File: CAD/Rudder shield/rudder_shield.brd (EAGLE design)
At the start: 49 x 19.7 mm, 8 parts

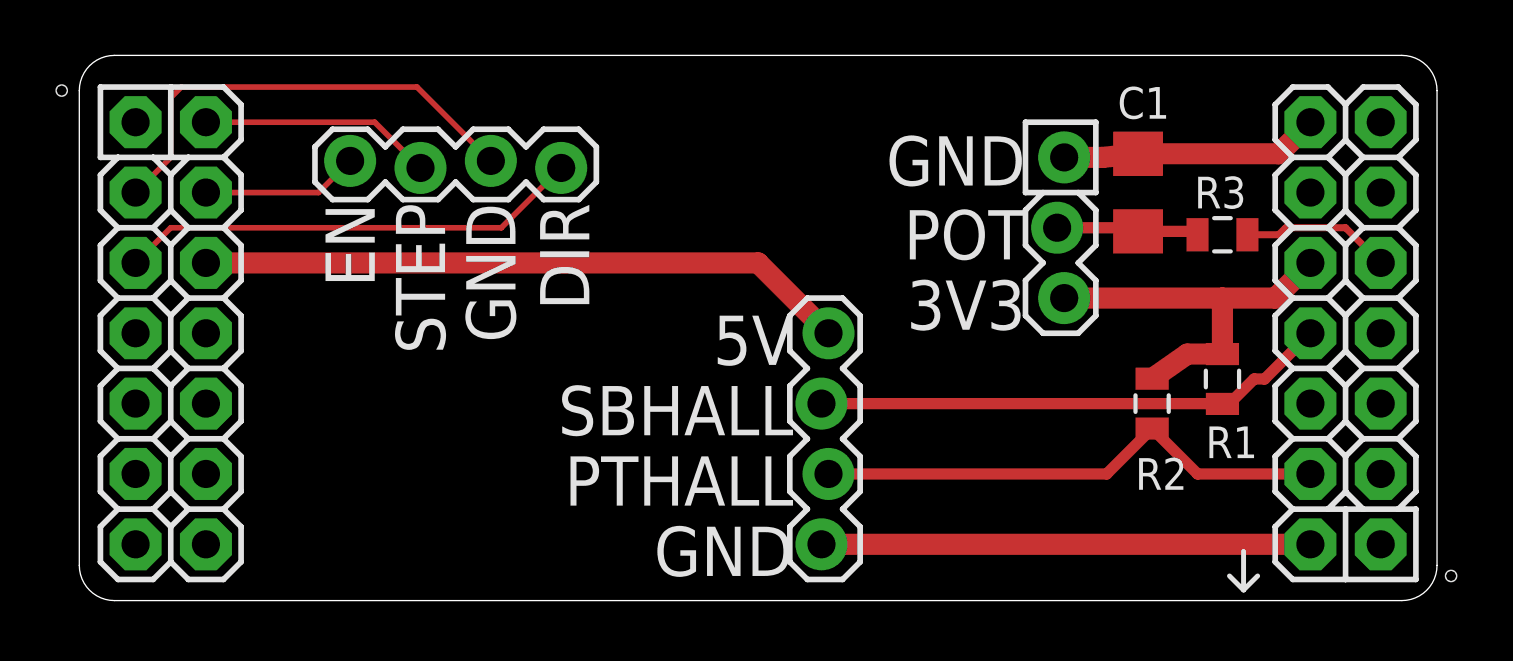
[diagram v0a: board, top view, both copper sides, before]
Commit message: Updated all CANode shields to fit the latest version of it.
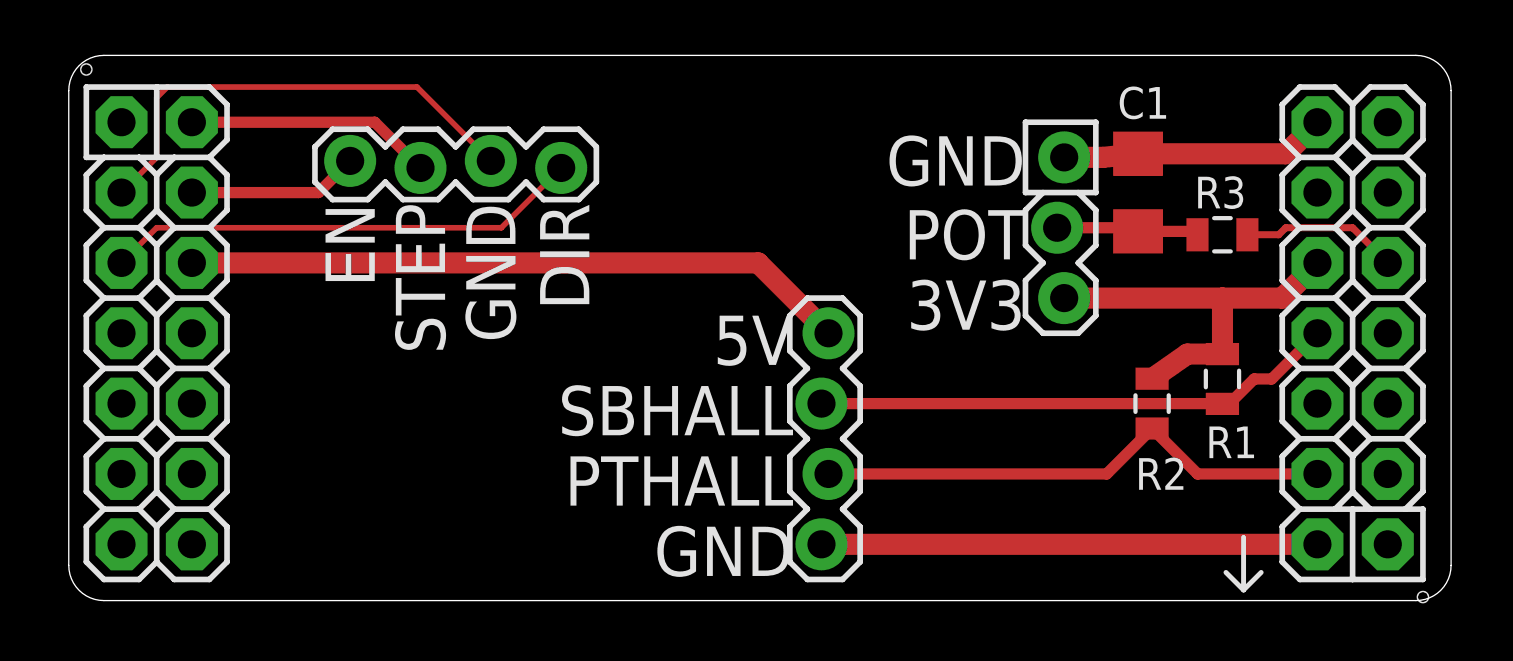
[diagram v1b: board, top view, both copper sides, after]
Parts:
- JP1: value (none) -> M03LOCK
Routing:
- net DIR: track 5.68 -> 6.19 mm
- net STEP: track 16.8 -> 17.3 mm
- net GND16: track 8.43 -> 8.94 mm
- net EN: track 16.8 -> 17.3 mm
- net 5V0: track 23.5 -> 24.0 mm
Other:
- board size 49 x 19.7 mm -> 49.9 x 19.7 mm
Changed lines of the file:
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@@
 <text x="34.544" y="20.955" size="1.778" layer="21" font="vector" ratio="12" rot="R180">POT</text>
 <text x="34.544" y="18.415" size="1.778" layer="21" font="vector" ratio="12" rot="R180">3V3</text>
-<wire x1="0.381" y1="25.273" x2="0.381" y2="8.128" width="0" layer="20"/>
-<wire x1="0.381" y1="8.128" x2="1.651" y2="6.858" width="0" layer="20" curve="90"/>
-<wire x1="1.651" y1="6.858" x2="48.133" y2="6.858" width="0" layer="20"/>
-<wire x1="48.133" y1="6.858" x2="49.403" y2="8.128" width="0" layer="20" curve="90"/>
-<wire x1="49.403" y1="8.128" x2="49.403" y2="25.273" width="0" layer="20"/>
-<wire x1="49.403" y1="25.273" x2="48.133" y2="26.543" width="0" layer="20" curve="90"/>
-<wire x1="48.133" y1="26.543" x2="1.651" y2="26.543" width="0" layer="20"/>
-<wire x1="1.651" y1="26.543" x2="0.381" y2="25.273" width="0" layer="20" curve="90"/>
-<wire x1="42.418" y1="7.239" x2="42.926" y2="7.747" width="0.1778" layer="21"/>
-<wire x1="42.418" y1="7.239" x2="41.91" y2="7.747" width="0.1778" layer="21"/>
-<wire x1="42.418" y1="7.366" x2="42.418" y2="8.636" width="0.1778" layer="21"/>
+<wire x1="0" y1="25.273" x2="0" y2="8.128" width="0" layer="20"/>
+<wire x1="0" y1="8.128" x2="1.27" y2="6.858" width="0" layer="20" curve="90"/>
+<wire x1="1.27" y1="6.858" x2="48.641" y2="6.858" width="0" layer="20"/>
+<wire x1="48.641" y1="6.858" x2="49.911" y2="8.128" width="0" layer="20" curve="90"/>
+<wire x1="49.911" y1="8.128" x2="49.911" y2="25.273" width="0" layer="20"/>
+<wire x1="49.911" y1="25.273" x2="48.641" y2="26.543" width="0" layer="20" curve="90"/>
+<wire x1="48.641" y1="26.543" x2="1.27" y2="26.543" width="0" layer="20"/>
+<wire x1="1.27" y1="26.543" x2="0" y2="25.273" width="0" layer="20" curve="90"/>
+<wire x1="42.418" y1="7.239" x2="43.053" y2="7.874" width="0.1778" layer="21"/>
+<wire x1="42.418" y1="7.239" x2="41.783" y2="7.874" width="0.1778" layer="21"/>
+<wire x1="42.418" y1="7.366" x2="42.418" y2="9.144" width="0.1778" layer="21"/>
 </plain>
 <attributes>
@@
 <elements>
 <element name="U$1" library="ASL" package="CANODE_SHIELD" value="CANODE_SHIELD" x="0" y="0"/>
-<element name="JP1" library="ASL" package="1X03_LOCK" value="" x="35.814" y="22.86" smashed="yes" rot="R270"/>
+<element name="JP1" library="ASL" package="1X03_LOCK" value="M03LOCK" x="35.814" y="22.86" smashed="yes" rot="R270"/>
 <element name="SL1" library="ASL" package="1X04_LOCK" value="" x="17.78" y="22.606" smashed="yes" rot="R180">
 <attribute name="VALUE" x="19.05" y="25.781" size="1.27" layer="27" rot="R180"/>
@@
 <contactref element="U$1" pad="RB2"/>
 <contactref element="R3" pad="2"/>
-<wire x1="46.101" y1="20.32" x2="47.371" y2="19.05" width="0.254" layer="1"/>
+<wire x1="46.355" y1="20.32" x2="47.625" y2="19.05" width="0.254" layer="1"/>
 <wire x1="42.556" y1="20.066" x2="43.688" y2="20.066" width="0.254" layer="1"/>
 <wire x1="43.688" y1="20.066" x2="43.942" y2="20.32" width="0.254" layer="1"/>
-<wire x1="43.942" y1="20.32" x2="46.101" y2="20.32" width="0.254" layer="1"/>
+<wire x1="43.942" y1="20.32" x2="46.355" y2="20.32" width="0.254" layer="1"/>
 </signal>
 <signal name="GND14">
@@
 <wire x1="37.335" y1="22.86" x2="38.608" y2="22.99" width="0.762" layer="1"/>
 <contactref element="U$1" pad="GND"/>
-<wire x1="38.608" y1="22.99" x2="43.691" y2="22.99" width="0.762" layer="1"/>
-<wire x1="43.691" y1="22.99" x2="44.831" y2="24.13" width="0.762" layer="1"/>
+<wire x1="38.608" y1="22.99" x2="43.945" y2="22.99" width="0.762" layer="1"/>
+<wire x1="43.945" y1="22.99" x2="45.085" y2="24.13" width="0.762" layer="1"/>
 </signal>
 <signal name="3V310">
@@
 <contactref element="R1" pad="2"/>
 <contactref element="R2" pad="2"/>
-<wire x1="41.656" y1="17.78" x2="43.561" y2="17.78" width="0.762" layer="1"/>
-<wire x1="43.561" y1="17.78" x2="44.831" y2="19.05" width="0.762" layer="1"/>
+<wire x1="41.656" y1="17.78" x2="43.815" y2="17.78" width="0.762" layer="1"/>
+<wire x1="43.815" y1="17.78" x2="45.085" y2="19.05" width="0.762" layer="1"/>
 <wire x1="41.656" y1="15.759" x2="41.656" y2="17.78" width="0.762" layer="1"/>
 <wire x1="39.116" y1="14.87" x2="40.386" y2="15.759" width="0.762" layer="1"/>
@@
 <contactref element="SL1" pad="1"/>
 <contactref element="U$1" pad="RB10"/>
-<wire x1="2.413" y1="19.05" x2="3.683" y2="20.32" width="0.2032" layer="1"/>
-<wire x1="3.683" y1="20.32" x2="15.621" y2="20.32" width="0.2032" layer="1"/>
+<wire x1="1.905" y1="19.05" x2="3.175" y2="20.32" width="0.2032" layer="1"/>
+<wire x1="3.175" y1="20.32" x2="15.621" y2="20.32" width="0.2032" layer="1"/>
 <wire x1="15.621" y1="20.32" x2="17.78" y2="22.479" width="0.2032" layer="1"/>
 </signal>
@@
 <contactref element="SL1" pad="4"/>
 <contactref element="U$1" pad="RB9"/>
-<wire x1="4.953" y1="21.59" x2="9.017" y2="21.59" width="0.2032" layer="1"/>
-<wire x1="9.017" y1="21.59" x2="10.16" y2="22.733" width="0.2032" layer="1"/>
+<wire x1="4.445" y1="21.59" x2="9.017" y2="21.59" width="0.4064" layer="1"/>
+<wire x1="9.017" y1="21.59" x2="10.16" y2="22.733" width="0.4064" layer="1"/>
 </signal>
 <signal name="5V0">
 <contactref element="SL2" pad="1"/>
 <contactref element="U$1" pad="5V1"/>
-<wire x1="4.953" y1="19.05" x2="24.892" y2="19.05" width="0.762" layer="1"/>
+<wire x1="4.445" y1="19.05" x2="24.892" y2="19.05" width="0.762" layer="1"/>
 <wire x1="24.892" y1="19.05" x2="27.432" y2="16.51" width="0.762" layer="1"/>
 </signal>
@@
 <contactref element="U$1" pad="RB1"/>
 <contactref element="R1" pad="1"/>
-<wire x1="43.18" y1="14.859" x2="44.831" y2="16.51" width="0.4064" layer="1"/>
+<wire x1="43.434" y1="14.859" x2="45.085" y2="16.51" width="0.4064" layer="1"/>
 <wire x1="41.91" y1="13.97" x2="41.656" y2="13.959" width="0.4064" layer="1"/>
 <wire x1="41.91" y1="13.97" x2="27.178" y2="13.97" width="0.4064" layer="1"/>
 <wire x1="41.91" y1="13.97" x2="42.799" y2="14.859" width="0.4064" layer="1"/>
-<wire x1="42.799" y1="14.859" x2="43.18" y2="14.859" width="0.4064" layer="1"/>
+<wire x1="42.799" y1="14.859" x2="43.434" y2="14.859" width="0.4064" layer="1"/>
 </signal>
 <signal name="PT_HALL">
@@
 <wire x1="37.476" y1="11.43" x2="39.116" y2="13.07" width="0.4064" layer="1"/>
 <wire x1="39.116" y1="13.07" x2="40.756" y2="11.43" width="0.4064" layer="1"/>
-<wire x1="40.756" y1="11.43" x2="44.831" y2="11.43" width="0.4064" layer="1"/>
+<wire x1="40.756" y1="11.43" x2="45.085" y2="11.43" width="0.4064" layer="1"/>
 </signal>
 <signal name="STEP" class="1">
 <contactref element="SL1" pad="2"/>
 <contactref element="U$1" pad="RB12"/>
-<wire x1="2.413" y1="21.59" x2="3.683" y2="22.86" width="0.2032" layer="1"/>
-<wire x1="3.683" y1="22.86" x2="3.683" y2="25.019" width="0.2032" layer="1"/>
-<wire x1="3.683" y1="25.019" x2="4.064" y2="25.4" width="0.2032" layer="1"/>
-<wire x1="4.064" y1="25.4" x2="12.573" y2="25.4" width="0.2032" layer="1"/>
+<wire x1="1.905" y1="21.59" x2="3.175" y2="22.86" width="0.2032" layer="1"/>
+<wire x1="3.175" y1="22.86" x2="3.175" y2="25.019" width="0.2032" layer="1"/>
+<wire x1="3.175" y1="25.019" x2="3.556" y2="25.4" width="0.2032" layer="1"/>
+<wire x1="3.556" y1="25.4" x2="12.573" y2="25.4" width="0.2032" layer="1"/>
 <wire x1="12.573" y1="25.4" x2="15.24" y2="22.733" width="0.2032" layer="1"/>
 </signal>
@@
 <contactref element="SL1" pad="3"/>
 <contactref element="U$1" pad="GND6"/>
-<wire x1="4.953" y1="24.13" x2="11.049" y2="24.13" width="0.2032" layer="1"/>
-<wire x1="11.049" y1="24.13" x2="12.7" y2="22.479" width="0.2032" layer="1"/>
+<wire x1="4.445" y1="24.13" x2="11.049" y2="24.13" width="0.4064" layer="1"/>
+<wire x1="11.049" y1="24.13" x2="12.7" y2="22.479" width="0.4064" layer="1"/>
 </signal>
 <signal name="GND2">
 <contactref element="SL2" pad="4"/>
 <contactref element="U$1" pad="GND2"/>
-<wire x1="27.178" y1="8.89" x2="44.831" y2="8.89" width="0.762" layer="1"/>
+<wire x1="27.178" y1="8.89" x2="45.085" y2="8.89" width="0.762" layer="1"/>
 </signal>
 <signal name="N$1">
